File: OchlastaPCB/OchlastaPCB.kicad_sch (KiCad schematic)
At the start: 1 part, among them U1 STM32F334R8Tx

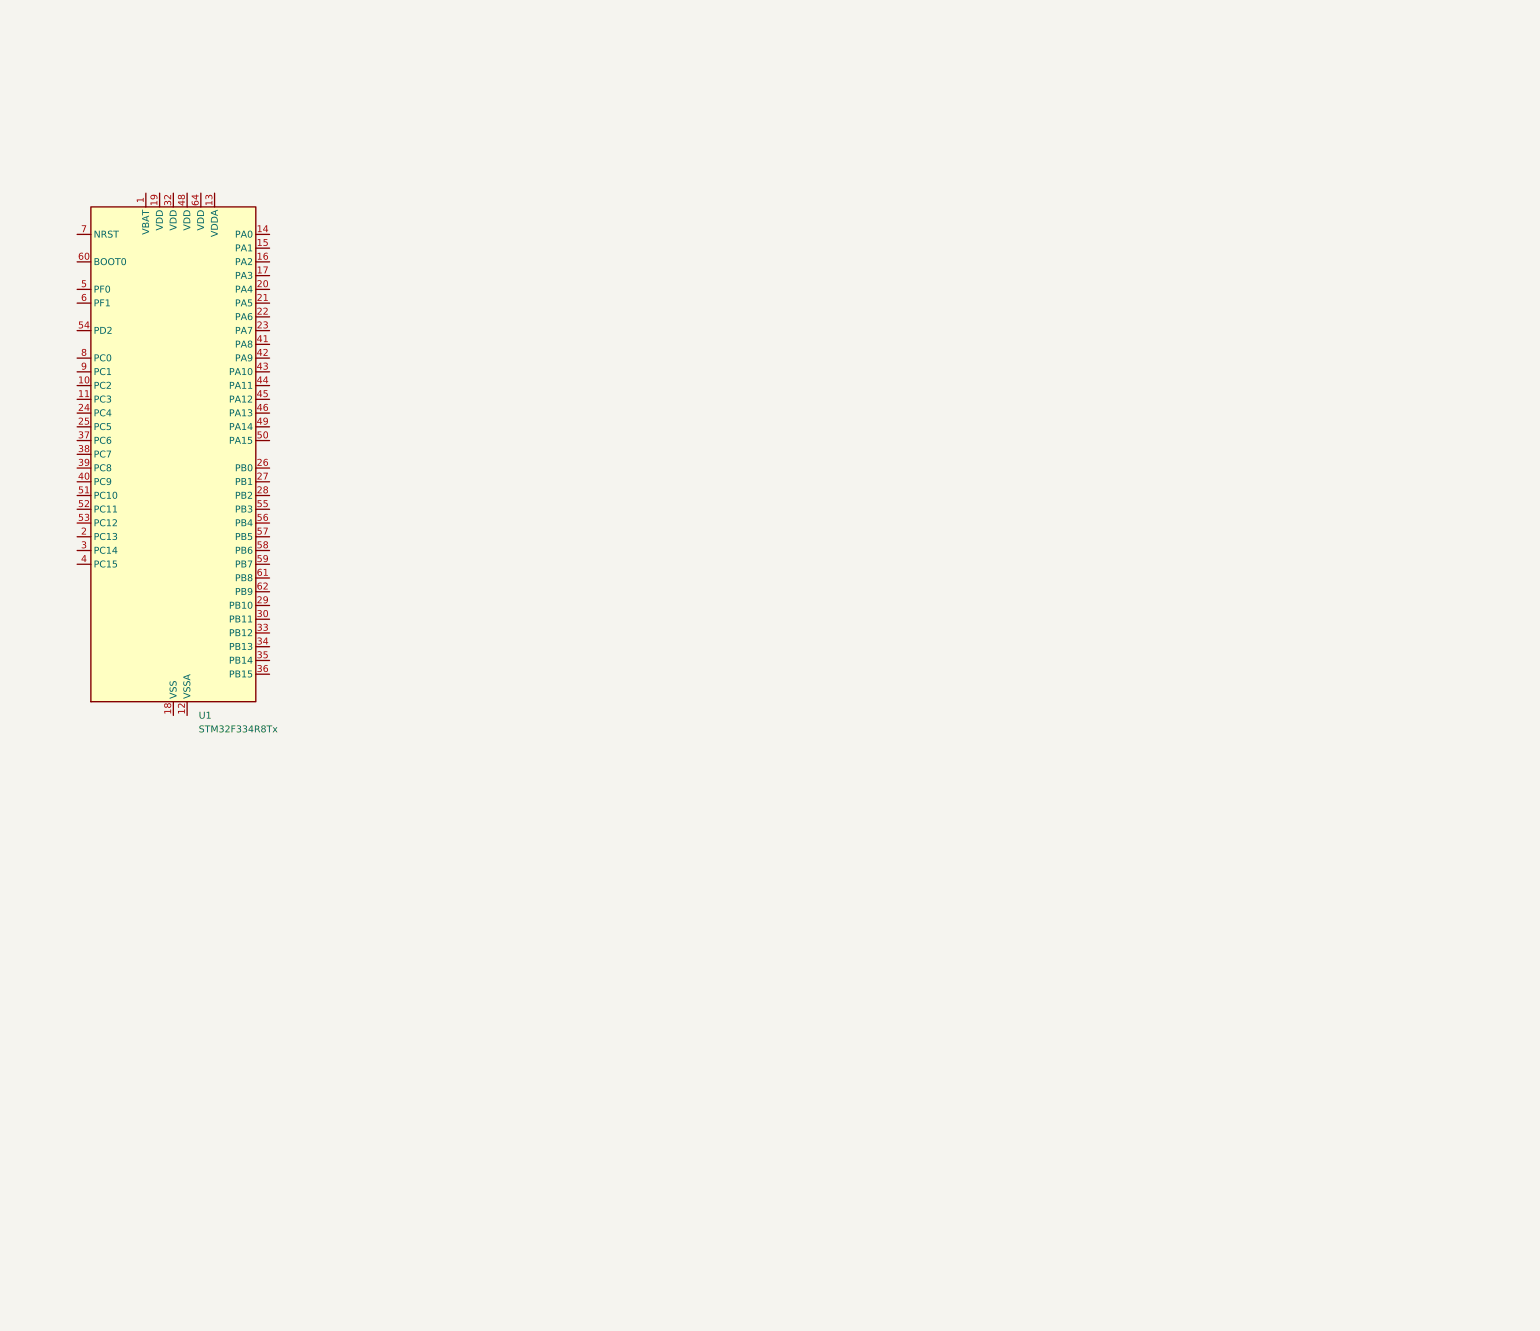
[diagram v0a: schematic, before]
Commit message: Power cascade for MCU schematics, created few components...
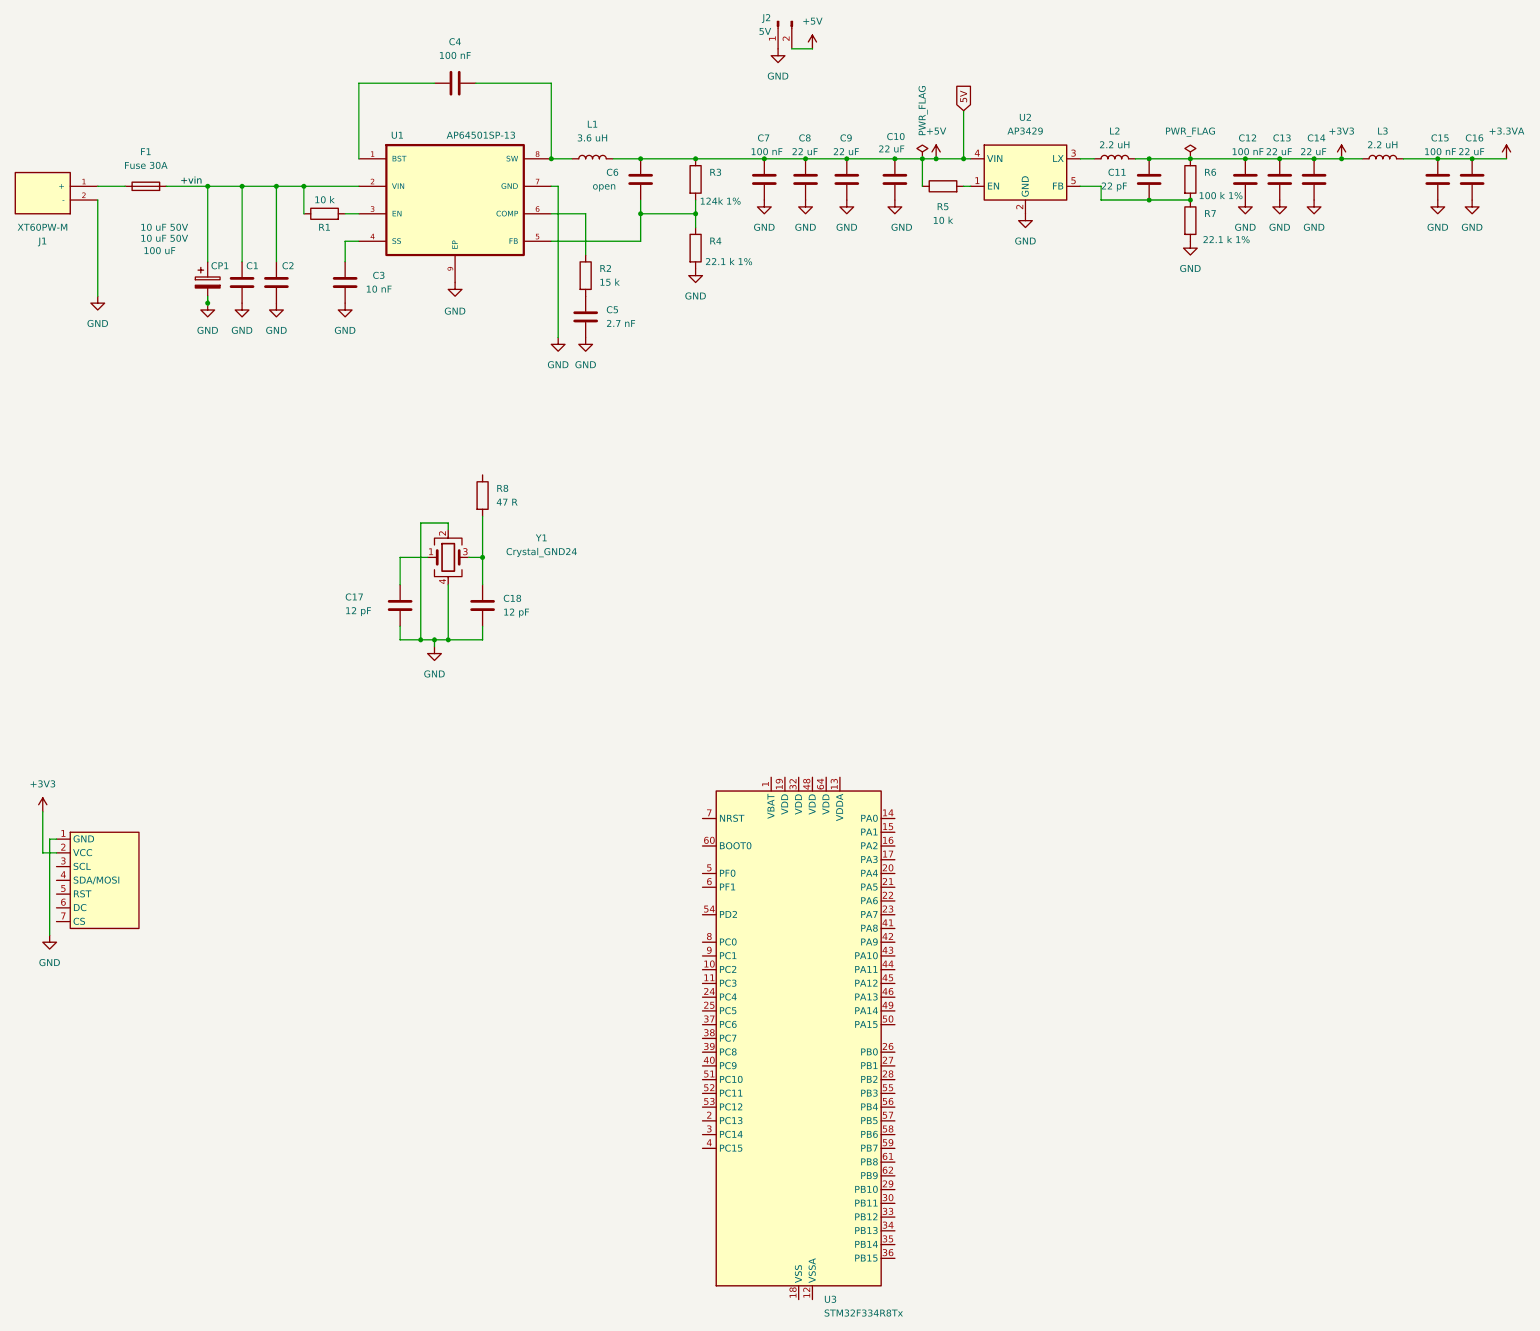
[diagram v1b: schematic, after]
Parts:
- added C1, C2: 10 uF 50V, Capacitor_SMD:C_1206_3216Metric, symbol Device:C
- added C10, C13, C14, C16, C8, C9: 22 uF, Capacitor_SMD:C_0805_2012Metric, symbol Device:C
- added C11: 22 pF, Capacitor_SMD:C_0603_1608Metric, symbol Device:C
- added C12, C15, C4, C7: 100 nF, Capacitor_SMD:C_0603_1608Metric, symbol Device:C
- added C17, C18: 12 pF, Capacitor_SMD:C_0603_1608Metric, symbol Device:C
- added C3: 10 nF, Capacitor_SMD:C_0603_1608Metric, symbol Device:C
- added C5: 2.7 nF, Capacitor_SMD:C_0603_1608Metric, symbol Device:C
- added C6: open, Capacitor_SMD:C_0603_1608Metric, symbol Device:C
- added CP1: 100 uF, Capacitor_SMD:CP_Elec_8x10, symbol Device:C_Polarized
- added F1: Fuse 30A, OchlastaFootprints:Fuseholder_Keystone_3557, symbol Device:Fuse
- added J1: XT60PW-M, SnapMagic_downloads:AMASS_XT60PW-M, symbol XT60PW-M:XT60PW-M
- added J2: 5V, Connector_PinHeader_2.54mm:PinHeader_1x02_P2.54mm_Vertical, symbol Connector:Conn_01x02_Pin
- added L1: 3.6 uH, Inductor_SMD:L_Changjiang_FNR4030S, symbol Device:L
- added L2, L3: 2.2 uH, Inductor_SMD:L_Changjiang_FNR3015S, symbol Device:L
- added R1, R5: 10 k, Resistor_SMD:R_0603_1608Metric, symbol Device:R
- added R2: 15 k, Resistor_SMD:R_0603_1608Metric, symbol Device:R
- added R3: 124k 1%, Resistor_SMD:R_0603_1608Metric, symbol Device:R
- added R4, R7: 22.1 k 1%, Resistor_SMD:R_0603_1608Metric, symbol Device:R
- added R6: 100 k 1%, Resistor_SMD:R_0603_1608Metric, symbol Device:R
- added R8: 47 R, Resistor_SMD:R_0603_1608Metric, symbol Device:R
- added TFT1: ~, OchlastaFootprints:GMT020-02 TFT Display, symbol OchlastaSymbols:GMT020-02_Display
- added U1: AP64501SP-13, SnapMagic_downloads:SOIC127P600X170-9N, symbol AP64501SP-13:AP64501SP-13
- added U2: AP3429, Package_TO_SOT_SMD:TSOT-23-5, symbol Greels symbol library:AP3429
- added Y1: Crystal_GND24, Crystal:Crystal_SMD_3225-4Pin_3.2x2.5mm, symbol Device:Crystal_GND24
- renumbered U1 to U3
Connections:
- new net: C11.2, R6.2, R7.1, U2.5 (FB)
- new net: C4.1, U1.1 (BST)
- new net: R1.2, U1.3 (EN)
- new net: C3.1, U1.4 (SS)
- new net: C6.2, R3.2, R4.1, U1.5 (FB)
- new net: R2.1, U1.6 (COMP)
- new net: C4.2, L1.1, U1.8 (SW)
- new net: C5.1, R2.2
- new net: C17.1, Y1.1
- new net: C18.1, R8.2, Y1.3
- new net: R5.2, U2.1 (EN)
- new net: L2.1, U2.3 (LX)
- new net: F1.1, J1.1 (+)
- new net +3.3VA: C15.1, C16.1, L3.2
- new net +3V3: C11.1, C12.1, C13.1, C14.1, L2.2, L3.1, R6.1, TFT1.2 (VCC)
- new net +5V: C10.1, C6.1, C7.1, C8.1, C9.1, J2.2 (Pin_2), L1.2, R3.1, R5.1, U2.4 (VIN)
- new net +vin: C1.1, C2.1, CP1.1, F1.2, R1.1, U1.2 (VIN)
- new net GND: C1.2, C10.2, C12.2, C13.2, C14.2, C15.2, C16.2, C17.2, C18.2, C2.2, C3.2, C5.2, C7.2, C8.2, C9.2, CP1.2, J1.2 (-), J2.1 (Pin_1), R4.2, R7.2, TFT1.1 (GND), U1.7 (GND), U1.9 (EP), U2.2 (GND), Y1.2, Y1.4
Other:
- company: (none) -> Trafopajka&Alkel Engineering
- title: (none) -> Ochlasta
- moved on the sheet: U3

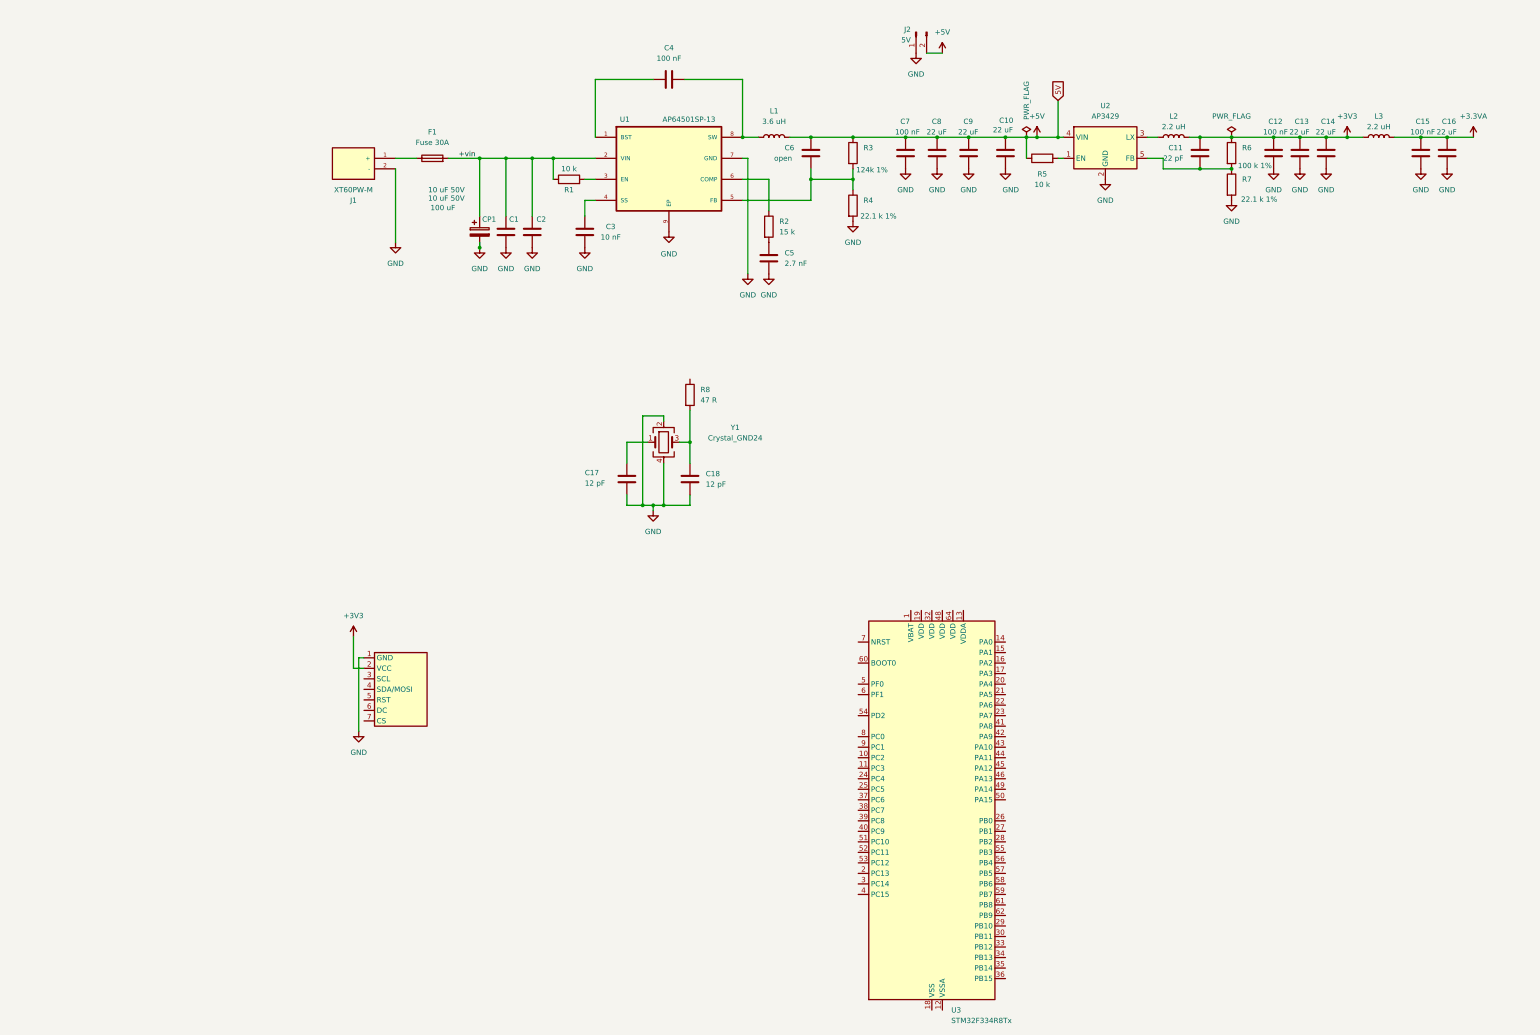
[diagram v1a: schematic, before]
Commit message: preliminary Pt1000 analog readout circuitry design and calculation in jupyter notebook
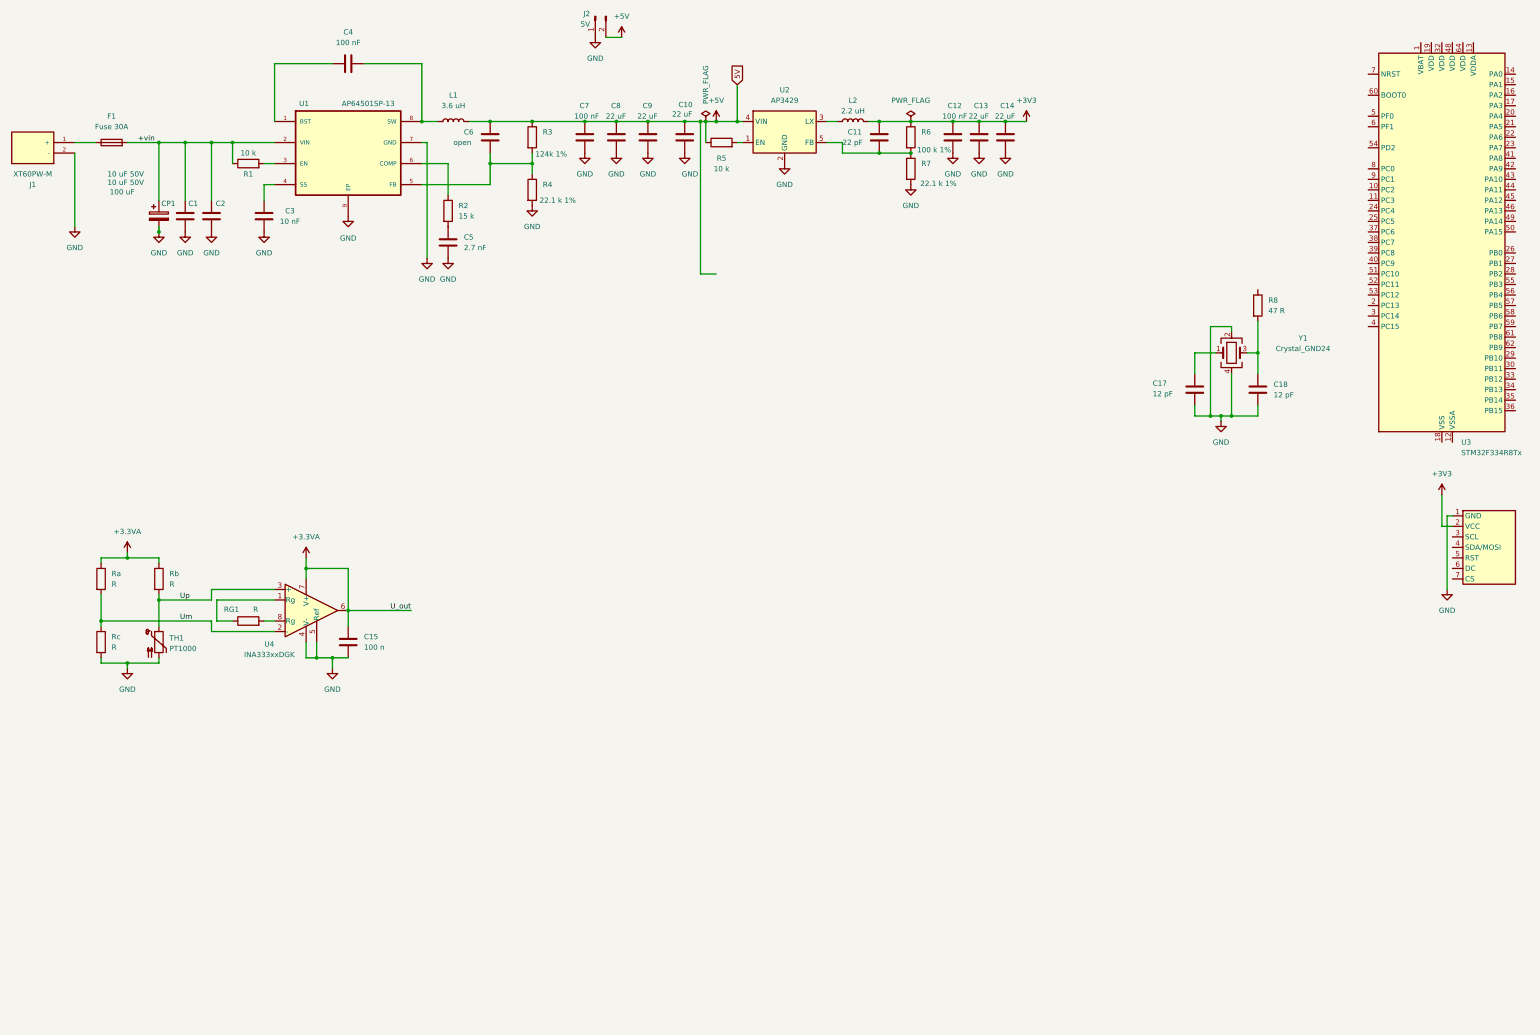
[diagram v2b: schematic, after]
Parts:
- removed C16: 22 uF, Capacitor_SMD:C_0805_2012Metric, symbol Device:C
- removed L3: 2.2 uH, Inductor_SMD:L_Changjiang_FNR3015S, symbol Device:L
- added RG1, Ra, Rb, Rc: R, symbol Device:R
- added TH1: PT1000, symbol Sensor_Temperature:PT1000
- added U4: INA333xxDGK, Package_SO:VSSOP-8_3x3mm_P0.65mm, symbol Amplifier_Instrumentation:INA333xxDGK
- C15: value 100 nF -> 100 n; footprint Capacitor_SMD:C_0603_1608Metric -> (none)
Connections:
- net +3.3VA: now also Ra.1, Rb.1, U4.6, U4.7 (V+)
- net GND: now also Rc.2, TH1.2, U4.4 (V-), U4.5 (Ref)
- new net: RG1.1, U4.1 (Rg)
- new net: RG1.2, U4.8 (Rg)
- new net Um: Ra.2, Rc.1, U4.2 (-)
- new net Up: Rb.2, TH1.1, U4.3 (+)
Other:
- moved on the sheet: C1, C10, C11, C12, C13, C14, C17, C18, C2, C3, C4, C5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
